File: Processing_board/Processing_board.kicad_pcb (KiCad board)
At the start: 4 copper layers, 95.2 x 62 mm, 148 parts, among them J1 Conn_01x08_Pin, J10 CONMHF1-SMD-G-T, J11 USB4215-03-A_REVA, J12 Conn_01x02_Pin, J2 Conn_01x08_Pin, J3 Conn_01x06_Pin, J4 Conn_01x03_Pin, J5 Conn_01x03_Pin, J6 Conn_01x02_Pin, Q1 DMP3056LSS-13, Q2 DMN66D0LT-7, Q3 DMN66D0LT-7, SW1 TL3305BF100QG, SW2 TL3305BF100QG, U1 STM32WBA63CIU6, U10 ADS1299IPAG, U11 ADS1299IPAG, U2 TPS7A7200RGW, U6 LD1117S33TR_SOT223, U9 MCP2200-I_SO

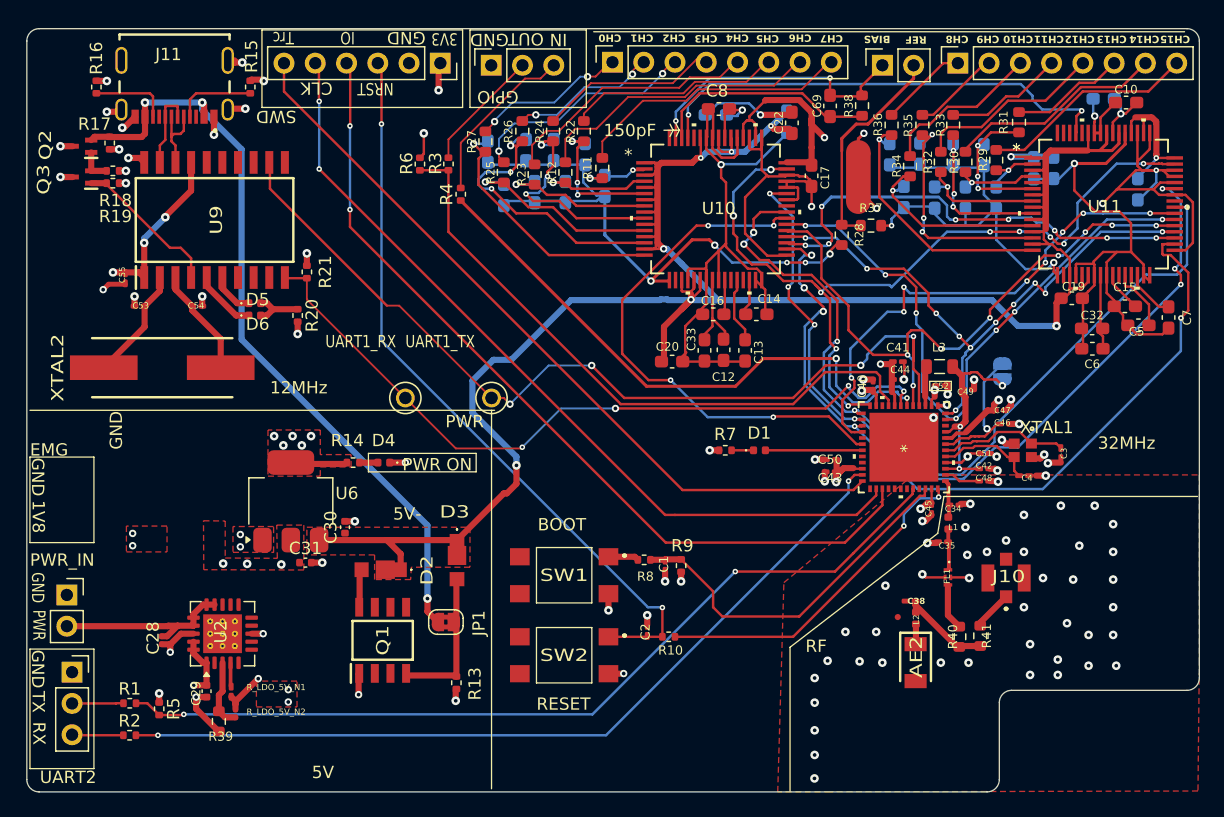
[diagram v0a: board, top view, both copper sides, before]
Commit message: feat: gerber files exported
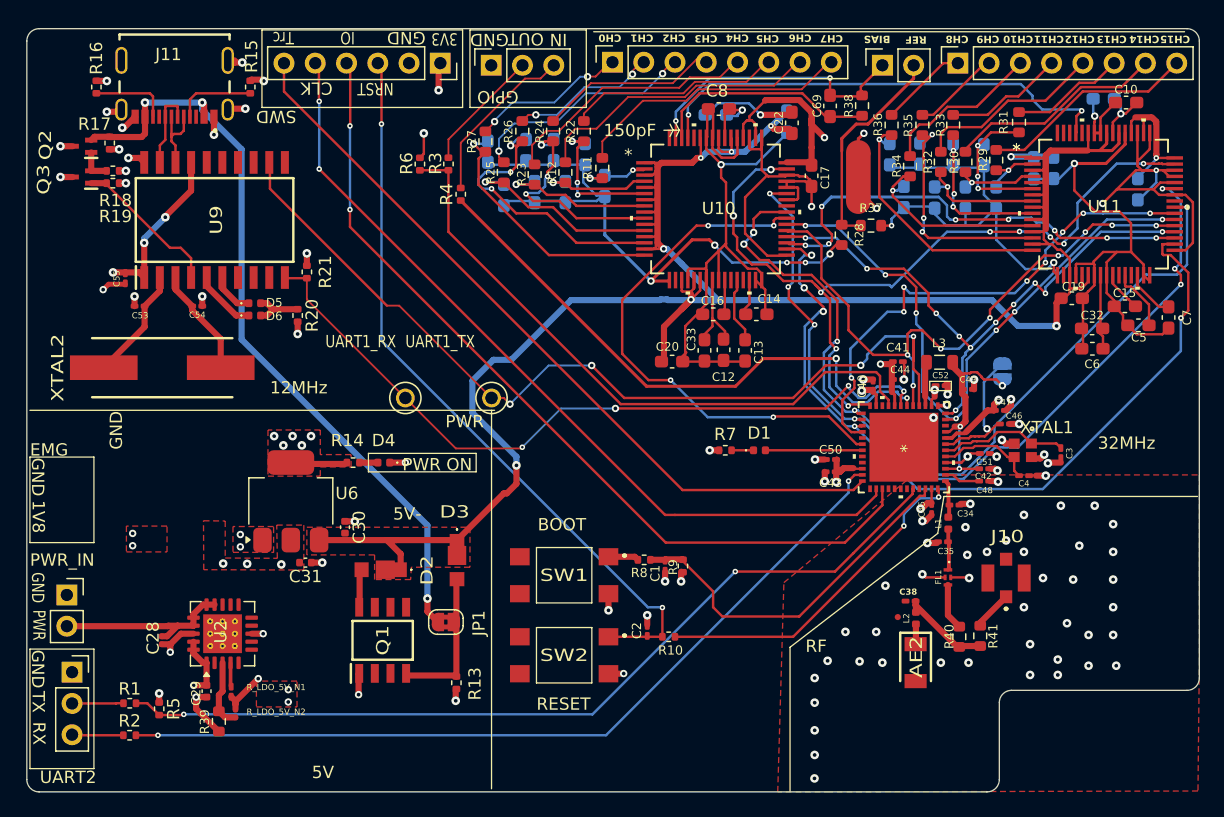
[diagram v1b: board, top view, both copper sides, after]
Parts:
- moved L3 0.35 mm to (152.9, 93.1)
- moved R9 0.15 mm to (132.1, 109.7)
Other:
- board text added: "alexandre"
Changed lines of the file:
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@@
 		(tags "capacitor handsolder")
 		(property "Reference" "C2"
-			(at 0.08 0.15 270)
+			(at -0.02 0.85 270)
 			(layer "F.SilkS")
 			(effects
@@
 		(tags "resistor")
 		(property "Reference" "R8"
-			(at -0.1 -1.35 0)
+			(at 0.4 -1.05 0)
 			(layer "F.SilkS")
 			(effects
@@
 		(tags "capacitor handsolder")
 		(property "Reference" "C35"
-			(at -0.325349 -0.317158 180)
+			(at -0.225349 -0.767158 180)
 			(layer "F.SilkS")
 			(effects
@@
 		(tags "resistor")
 		(property "Reference" "R41"
-			(at 0 -0.5225 90)
+			(at 0.023122 -1.049172 90)
 			(layer "F.SilkS")
 			(effects
@@
 		(tags "inductor")
 		(property "Reference" "L2"
-			(at 0.110842 -0.023503 90)
+			(at 0.010842 0.776497 90)
 			(layer "F.SilkS")
 			(effects
@@
 		(tags "capacitor handsolder")
 		(property "Reference" "C5"
-			(at -0.146267 0.51 0)
+			(at 0.038438 0.985966 0)
 			(layer "F.SilkS")
 			(effects
@@
 		(tags "capacitor handsolder")
 		(property "Reference" "C43"
-			(at 0.050466 -0.5 180)
+			(at 0.000466 -0.9 180)
 			(layer "F.SilkS")
 			(effects
 				(font
-					(size 0.75 0.75)
+					(size 0.7 0.7)
 					(thickness 0.15)
 				)
@@
 		(tags "capacitor handsolder")
 		(property "Reference" "C34"
-			(at -0.105 0.302 0)
+			(at 0.895 0.702 0)
 			(layer "F.SilkS")
 			(effects
@@
 		(tags "capacitor handsolder")
 		(property "Reference" "C4"
-			(at -0.24 -0.19 180)
+			(at 0.01 -0.64 180)
 			(layer "F.SilkS")
 			(effects
@@
 		(tags "capacitor handsolder")
 		(property "Reference" "C15"
-			(at 0 -1.55 0)
+			(at -0.028168 -1.074957 0)
 			(layer "F.SilkS")
 			(effects
@@
 		(tags "capacitor handsolder")
 		(property "Reference" "C45"
-			(at -0.02 0.25 90)
+			(at 0.03 0.8 270)
 			(layer "F.SilkS")
 			(effects
@@
 		(tags "Filter")
 		(property "Reference" "FL1"
-			(at -0.075842 0.074651 90)
+			(at -0.025842 0.774651 90)
 			(layer "F.SilkS")
 			(effects
@@
 		(tags "capacitor handsolder")
 		(property "Reference" "C38"
-			(at -0.4575 0 180)
+			(at 0.1925 0.75 180)
 			(layer "F.SilkS")
 			(effects
@@
 		(tags "capacitor handsolder")
 		(property "Reference" "C46"
-			(at 0.21 0.11 180)
+			(at -0.74 0.66 180)
 			(layer "F.SilkS")
 			(effects
@@
 		(tags "resistor")
 		(property "Reference" "R39"
-			(at 1.225 -0.15 180)
+			(at 0.025 1.15 270)
 			(layer "F.SilkS")
 			(effects
@@
 		(tags "capacitor handsolder")
 		(property "Reference" "C50"
-			(at -0.070466 0 0)
+			(at -0.020466 -0.8 0)
 			(layer "F.SilkS")
 			(effects
 				(font
-					(size 0.75 0.75)
+					(size 0.7 0.7)
 					(thickness 0.15)
 				)
@@
 	(footprint "Resistor_SMD:R_0402_1005Metric"
 		(layer "F.Cu")
-		(at 131.9 109.62 90)
+		(at 132.05 109.65 90)
 		(descr "Resistor SMD 0402 (1005 Metric), square (rectangular) end terminal, IPC_7351 nominal, (Body size source: IPC-SM-782 page 72, https://www.pcb-3d.com/wordpress/wp-content/uploads/ipc-sm-782a_amendment_1_and_2.pdf), generated with kicad-footprint-generator")
 		(tags "resistor")
 		(property "Reference" "R9"
-			(at 1.62 0.1 180)
+			(at -0.1 -0.8 270)
 			(layer "F.SilkS")
 			(effects
 				(font
-					(size 1 1)
+					(size 0.7 0.7)
 					(thickness 0.153)
 				)
@@
 		(tags "Integrated Circuit")
 		(property "Reference" "J10"
-			(at -0.200349 0.125842 0)
+			(at -0.100349 3.375842 0)
 			(layer "F.SilkS")
 			(effects
@@
 		(tags "capacitor handsolder")
 		(property "Reference" "C1"
-			(at 0.125 -0.1 90)
+			(at -0.625 -0.8 90)
 			(layer "F.SilkS")
 			(effects
@@
 	(footprint "Inductor_SMD:L_0805_2012Metric"
 		(layer "F.Cu")
-		(at 152.9 93.45 180)
+		(at 152.9 93.1 180)
 		(descr "Inductor SMD 0805 (2012 Metric), square (rectangular) end terminal, IPC_7351 nominal, (Body size source: IPC-SM-782 page 80, https://www.pcb-3d.com/wordpress/wp-content/uploads/ipc-sm-782a_amendment_1_and_2.pdf), generated with kicad-footprint-generator")
 		(tags "inductor")
@@
 		(tags "capacitor handsolder")
 		(property "Reference" "C51"
-			(at 0.07 0.01 180)
+			(at 0.02 -0.69 180)
 			(layer "F.SilkS")
 			(effects
@@
 		(tags "capacitor handsolder")
 		(property "Reference" "C48"
-			(at 0.02 0.25 180)
+			(at -0.03 -0.75 180)
 			(layer "F.SilkS")
 			(effects
@@
 		(tags "capacitor handsolder")
 		(property "Reference" "C47"
-			(at -0.2 0.01 180)
+			(at -0.25 0.66 180)
 			(layer "F.SilkS")
 			(effects
@@
 		(tags "capacitor handsolder")
 		(property "Reference" "C52"
-			(at 0.005 -0.025 180)
+			(at 0.001801 0.83564 180)
 			(layer "F.SilkS")
 			(effects
@@
 		(tags "capacitor")
 		(property "Reference" "C31"
-			(at 0 -1.16 0)
+			(at 0 1.125 0)
 			(layer "F.SilkS")
 			(effects
@@
 		(tags "inductor")
 		(property "Reference" "L1"
-			(at 0.332158 -0.395349 180)
+			(at 0.032158 0.804651 270)
 			(layer "F.SilkS")
 			(effects
@@
 		(tags "capacitor")
 		(property "Reference" "C30"
-			(at 0 -1.16 90)
+			(at 0 1.155 90)
 			(layer "F.SilkS")
 			(effects
@@
 		(tags "capacitor handsolder")
 		(property "Reference" "C42"
-			(at 0.02 0.25 180)
+			(at 0.07 -0.6 180)
 			(layer "F.SilkS")
 			(effects
@@
 		(tags "LED")
 		(property "Reference" "D5"
-			(at 0.235 -0.3 0)
+			(at 1.585 -0.05 0)
 			(layer "F.SilkS")
 			(effects
 				(font
-					(size 1 1)
+					(size 0.7 0.7)
 					(thickness 0.153)
 				)
@@
 		(tags "LED")
 		(property "Reference" "D6"
-			(at 0.235 0.7 0)
+			(at 1.585 0.05 0)
 			(layer "F.SilkS")
 			(effects
 				(font
-					(size 1 1)
+					(size 0.7 0.7)
 					(thickness 0.153)
 				)
@@
 		(tags "resistor")
 		(property "Reference" "R40"
-			(at 0 0.5225 90)
+			(at -0.018269 0.813385 90)
 			(layer "F.SilkS")
 			(effects
@@
 		(tags "capacitor handsolder")
 		(property "Reference" "C54"
-			(at 0.0925 0.04 180)
+			(at -0.0075 -0.71 180)
 			(layer "F.SilkS")
 			(effects
@@
 		(tags "capacitor handsolder")
 		(property "Reference" "C53"
-			(at 0.0925 -0.04 0)
+			(at 0.0425 0.76 0)
 			(layer "F.SilkS")
 			(effects
@@
 		(tags "capacitor handsolder")
 		(property "Reference" "C55"
-			(at -0.28 0.25 270)
+			(at 0.02 0.7 270)
 			(layer "F.SilkS")
 			(effects
@@
 		(tags "capacitor handsolder")
 		(property "Reference" "C3"
-			(at 0.025 -0.25 270)
+			(at 0.025 -0.7 270)
 			(layer "F.SilkS")
 			(effects
@@
 		(tags "capacitor handsolder")
 		(property "Reference" "C49"
-			(at 0.2 -0.2 180)
+			(at 0 0.8 180)
 			(layer "F.SilkS")
 			(effects
@@
 		)
 	)
+	(gr_text "alexandre"
+		(at 157.9 98.15 90)
+		(layer "B.SilkS")
+		(effects
+			(font
+				(size 1 1)
+				(thickness 0.153)
+			)
+			(justify left bottom mirror)
+		)
+	)
 	(gr_text "marta"
 		(at 161.25 98.15 90)
@@
 	)
 	(segment
-		(start 151.701315 103.951)
-		(end 151.299 103.951)
+		(start 134.5 113)
+		(end 134.5 111.71)
 		(width 0.2)
 		(layer "F.Cu")
@@
 	)
 	(segment
-		(start 134.5 113)
-		(end 134.5 111.71)
-		(width 0.2)
+		(start 132.05 109.14)
+		(end 132.02 109.11)
+		(width 0.5)
 		(layer "F.Cu")
 		(net 3)
 	)
 	(segment
-		(start 151.701315 103.424126)
-		(end 151.701315 103.951)
-		(width 0.2)
+		(start 130.6 109.145)
+		(end 129.415 109.145)
+		(width 0.5)
 		(layer "F.Cu")
 		(net 3)
 	)
 	(segment
-		(start 134.5 111.71)
-		(end 131.9 109.11)
+		(start 151.299 103.951)
+		(end 141.5 113.75)
 		(width 0.2)
 		(layer "F.Cu")
@@
 	)
 	(segment
-		(start 130.6 109.145)
-		(end 129.415 109.145)
+		(start 132.02 109.11)
+		(end 130.635 109.11)
 		(width 0.5)
 		(layer "F.Cu")
@@
 	)
 	(segment
-		(start 151.299 103.951)
-		(end 141.5 113.75)
+		(start 141.5 113.75)
+		(end 135.25 113.75)
 		(width 0.2)
 		(layer "F.Cu")
@@
 	)
 	(segment
-		(start 131.9 109.11)
-		(end 130.635 109.11)
+		(start 129.415 109.145)
+		(end 129.41 109.15)
 		(width 0.5)
 		(layer "F.Cu")
@@
 	)
 	(segment
-		(start 141.5 113.75)
-		(end 135.25 113.75)
+		(start 132.05 109.26)
+		(end 132.05 109.14)
+		(width 0.2)
+		(layer "F.Cu")
+		(net 3)
+	)
+	(segment
+		(start 151.701315 103.951)
+		(end 151.299 103.951)
+		(width 0.2)
+		(layer "F.Cu")
+		(net 3)
+	)
+	(segment
+		(start 151.701315 103.424126)
+		(end 151.701315 103.951)
 		(width 0.2)
 		(layer "F.Cu")
@@
 	)
 	(segment
-		(start 129.415 109.145)
-		(end 129.41 109.15)
-		(width 0.5)
+		(start 134.5 111.71)
+		(end 132.05 109.26)
+		(width 0.2)
 		(layer "F.Cu")
 		(net 3)
@@
 	)
 	(segment
-		(start 153.9625 93.45)
-		(end 154.72 94.2075)
-		(width 0.5)
-		(layer "F.Cu")
-		(net 10)
-	)
-	(segment
 		(start 156.97 98.72)
 		(end 157.58 98.11)
@@
 	)
 	(segment
+		(start 153.9625 93.1)
+		(end 153.9625 93.45)
+		(width 0.5)
+		(layer "F.Cu")
+		(net 10)
+	)
+	(segment
 		(start 154.281563 99.504973)
 		(end 154.281563 99.504972)
@@
 	)
 	(segment
+		(start 153.9625 93.45)
+		(end 154.72 94.2075)
+		(width 0.5)
+		(layer "F.Cu")
+		(net 10)
+	)
+	(segment
 		(start 155.360057 94)
 		(end 154.9275 94)
@@
 		(width 0.5)
 		(layer "F.Cu")
+		(net 27)
+	)
+	(segment
+		(start 151.8375 93.1)
+		(end 151.8375 93.45)
+		(width 0.5)
+		(layer "F.Cu")
